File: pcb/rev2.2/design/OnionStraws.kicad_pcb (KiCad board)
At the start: 2 copper layers, 88.6 x 30 mm, 74 parts, among them J1 8P8C, J2 1x6, J3 TC2030, Q1 Si2309CDS, Q2 Si2309CDS, SW1 SW_Push, SW2 SW_Push, U1 APX803L20-29SA-7, U2 ESP32-C3-WROOM-02, U3 L7805, U4 74LVC2G07, U5 74LVC2G07_3v3, U6 AP2205-3.3

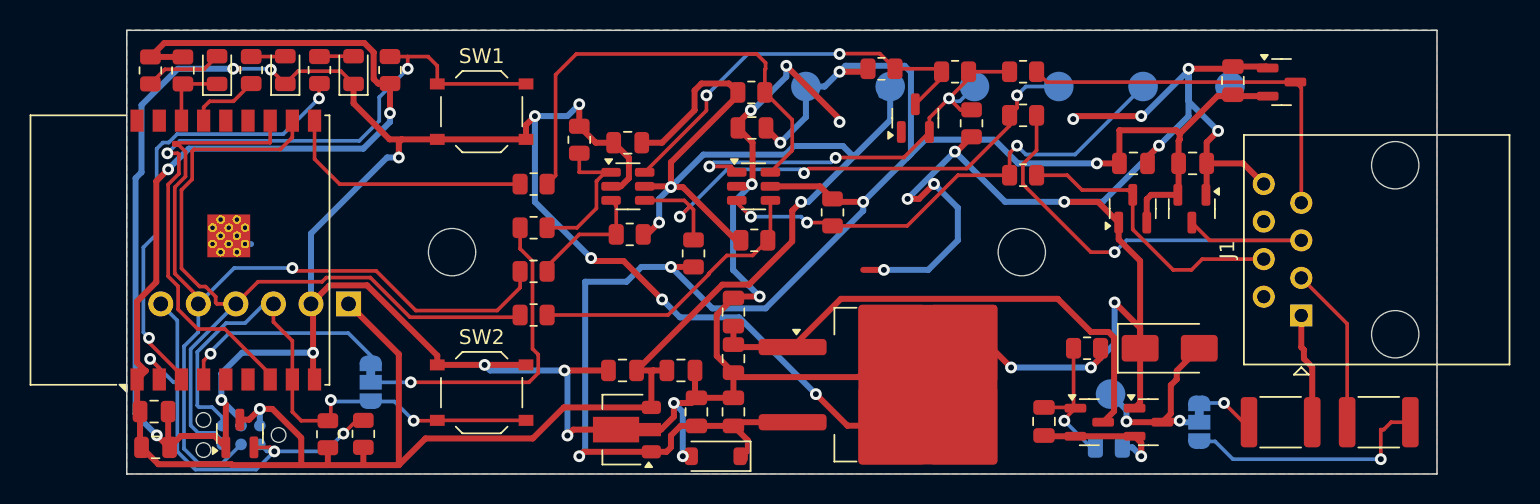
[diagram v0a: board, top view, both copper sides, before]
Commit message: fix(pcb): stage reviewed historical Rev2.2 source
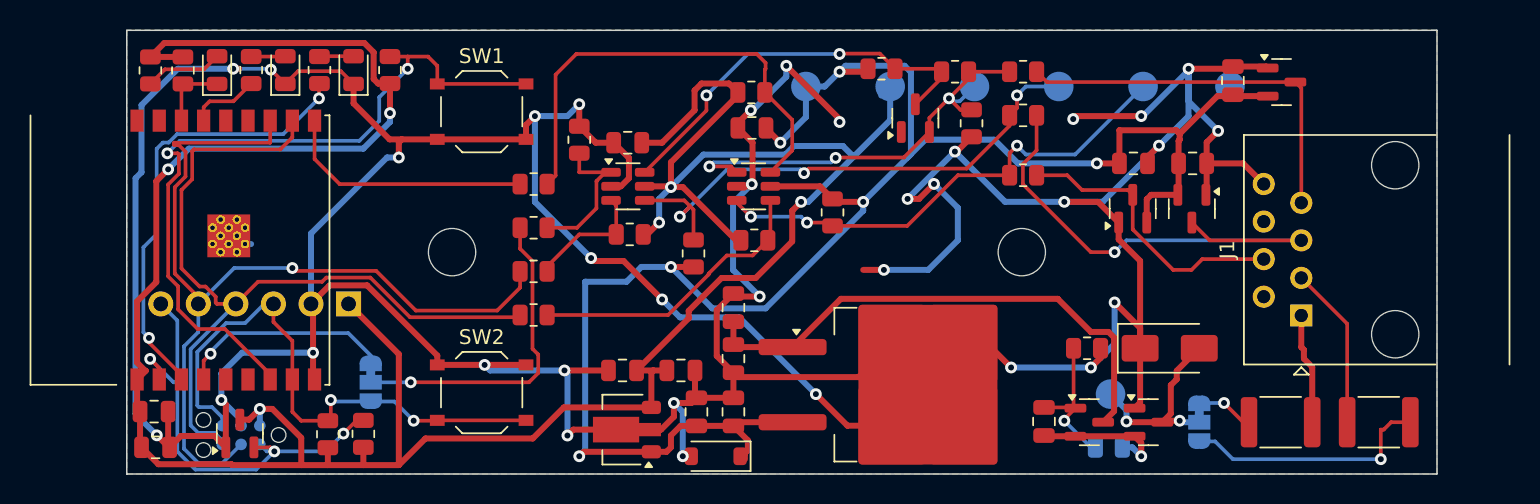
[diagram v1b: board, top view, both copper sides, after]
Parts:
- C1: footprint Capacitor_SMD:C_0805_2012Metric -> LegacyBoard:C1_C_0805_2012Metric
- C10: footprint Capacitor_SMD:C_0805_2012Metric -> LegacyBoard:C10_C_0805_2012Metric
- C11: footprint Capacitor_SMD:C_0805_2012Metric -> LegacyBoard:C11_C_0805_2012Metric
- C12: footprint Capacitor_SMD:C_0805_2012Metric -> LegacyBoard:C12_C_0805_2012Metric
- C13: footprint Capacitor_SMD:C_0805_2012Metric -> LegacyBoard:C13_C_0805_2012Metric
- C14: footprint Capacitor_SMD:C_0805_2012Metric -> LegacyBoard:C14_C_0805_2012Metric
- C2: footprint Capacitor_SMD:C_0805_2012Metric -> LegacyBoard:C2_C_0805_2012Metric
- C3: footprint Capacitor_SMD:C_0805_2012Metric -> LegacyBoard:C3_C_0805_2012Metric
- C4: footprint Capacitor_SMD:C_0805_2012Metric -> LegacyBoard:C4_C_0805_2012Metric
- C5: footprint Capacitor_SMD:C_0805_2012Metric -> LegacyBoard:C5_C_0805_2012Metric
- C6: footprint Capacitor_SMD:C_0805_2012Metric -> LegacyBoard:C6_C_0805_2012Metric
- C7: footprint Capacitor_SMD:C_0805_2012Metric -> LegacyBoard:C7_C_0805_2012Metric
- C8: footprint Capacitor_SMD:C_0805_2012Metric -> LegacyBoard:C8_C_0805_2012Metric
- C9: footprint Capacitor_SMD:C_0805_2012Metric -> LegacyBoard:C9_C_0805_2012Metric
- D1: footprint Package_TO_SOT_SMD:SOT-23 -> LegacyBoard:D1_SOT-23
- D2: footprint Package_TO_SOT_SMD:SOT-23 -> LegacyBoard:D2_SOT-23
- D3: footprint Package_TO_SOT_SMD:SOT-23 -> LegacyBoard:D3_SOT-23
- D4: footprint LED_SMD:LED_0805_2012Metric -> LegacyBoard:D4_LED_0805_2012Metric
- D5: footprint LED_SMD:LED_0805_2012Metric -> LegacyBoard:D5_LED_0805_2012Metric
- D6: footprint LED_SMD:LED_0805_2012Metric -> LegacyBoard:D6_LED_0805_2012Metric
- D7: footprint Diode_SMD:D_SMA -> LegacyBoard:D7_D_SMA
- D8: footprint Diode_SMD:D_SOD-123 -> LegacyBoard:D8_D_SOD-123
- D9: footprint Package_TO_SOT_SMD:SOT-23 -> LegacyBoard:D9_SOT-23
- F1: footprint Fuse:Fuse_1812_4532Metric -> LegacyBoard:F1_Fuse_1812_4532Metric
- F2: footprint Fuse:Fuse_1812_4532Metric -> LegacyBoard:F2_Fuse_1812_4532Metric
- H1: footprint MountingHole:MountingHole_3.2mm_M3_DIN965 -> LegacyBoard:H1_MountingHole_3.2mm_M3_DIN965
- H2: footprint MountingHole:MountingHole_3.2mm_M3_DIN965 -> LegacyBoard:H2_MountingHole_3.2mm_M3_DIN965
- J1: footprint OnionStraws:RJ45_EVERCOM_5301-8P8C_Horizontal -> LegacyBoard:J1_RJ45_EVERCOM_5301-8P8C_Horizontal
- J2: footprint Connector_PinHeader_2.54mm:PinHeader_1x06_P2.54mm_Vertical -> LegacyBoard:J2_PinHeader_1x06_P2.54mm_Vertical
- J3: footprint Connector:Tag-Connect_TC2030-IDC-NL_2x03_P1.27mm_Vertical -> LegacyBoard:J3_Tag-Connect_TC2030-IDC-NL_2x03_P1.27mm_Vertical
- JP1: footprint Jumper:SolderJumper-3_P1.3mm_Bridged12_RoundedPad1.0x1.5mm_NumberLabels -> LegacyBoard:JP1_SolderJumper-3_P1.3mm_Bridged12_RoundedPad1.0x1.5mm_NumberLabels
- JP2: footprint Jumper:SolderJumper-3_P1.3mm_Bridged12_RoundedPad1.0x1.5mm_NumberLabels -> LegacyBoard:JP2_SolderJumper-3_P1.3mm_Bridged12_RoundedPad1.0x1.5mm_NumberLabels
- Q1: footprint Package_TO_SOT_SMD:SOT-23 -> LegacyBoard:Q1_SOT-23
- Q2: footprint Package_TO_SOT_SMD:SOT-23 -> LegacyBoard:Q2_SOT-23
- R1: footprint Resistor_SMD:R_0805_2012Metric -> LegacyBoard:R1_R_0805_2012Metric
- R10: footprint Resistor_SMD:R_0805_2012Metric -> LegacyBoard:R10_R_0805_2012Metric
- R11: footprint Resistor_SMD:R_0805_2012Metric -> LegacyBoard:R11_R_0805_2012Metric
- R12: footprint Resistor_SMD:R_0805_2012Metric -> LegacyBoard:R12_R_0805_2012Metric
- R13: footprint Resistor_SMD:R_0805_2012Metric -> LegacyBoard:R13_R_0805_2012Metric
- R14: footprint Resistor_SMD:R_0805_2012Metric -> LegacyBoard:R14_R_0805_2012Metric
- R15: footprint Resistor_SMD:R_0805_2012Metric -> LegacyBoard:R15_R_0805_2012Metric
- R16: footprint Resistor_SMD:R_0805_2012Metric -> LegacyBoard:R16_R_0805_2012Metric
- R17: footprint Resistor_SMD:R_0805_2012Metric -> LegacyBoard:R17_R_0805_2012Metric
- R18: footprint Resistor_SMD:R_0805_2012Metric -> LegacyBoard:R18_R_0805_2012Metric
- R19: footprint Resistor_SMD:R_0805_2012Metric -> LegacyBoard:R19_R_0805_2012Metric
- R2: footprint Resistor_SMD:R_0805_2012Metric -> LegacyBoard:R2_R_0805_2012Metric
- R20: footprint Resistor_SMD:R_0805_2012Metric -> LegacyBoard:R20_R_0805_2012Metric
- R21: footprint Resistor_SMD:R_0805_2012Metric -> LegacyBoard:R21_R_0805_2012Metric
- R22: footprint Resistor_SMD:R_0805_2012Metric -> LegacyBoard:R22_R_0805_2012Metric
- R23: footprint Resistor_SMD:R_0805_2012Metric -> LegacyBoard:R23_R_0805_2012Metric
- R24: footprint Resistor_SMD:R_0805_2012Metric -> LegacyBoard:R24_R_0805_2012Metric
- R25: footprint Resistor_SMD:R_0805_2012Metric -> LegacyBoard:R25_R_0805_2012Metric
- R3: footprint Resistor_SMD:R_0805_2012Metric -> LegacyBoard:R3_R_0805_2012Metric
- R4: footprint Resistor_SMD:R_0805_2012Metric -> LegacyBoard:R4_R_0805_2012Metric
- R5: footprint Resistor_SMD:R_0805_2012Metric -> LegacyBoard:R5_R_0805_2012Metric
- R6: footprint Resistor_SMD:R_0805_2012Metric -> LegacyBoard:R6_R_0805_2012Metric
- R7: footprint Resistor_SMD:R_0805_2012Metric -> LegacyBoard:R7_R_0805_2012Metric
- R8: footprint Resistor_SMD:R_0805_2012Metric -> LegacyBoard:R8_R_0805_2012Metric
- R9: footprint Resistor_SMD:R_0805_2012Metric -> LegacyBoard:R9_R_0805_2012Metric
- SW1: footprint Button_Switch_SMD:SW_Push_1P1T_XKB_TS-1187A -> LegacyBoard:SW1_SW_Push_1P1T_XKB_TS-1187A
- SW2: footprint Button_Switch_SMD:SW_Push_1P1T_XKB_TS-1187A -> LegacyBoard:SW2_SW_Push_1P1T_XKB_TS-1187A
- TP1: footprint TestPoint:TestPoint_Pad_D2.0mm -> LegacyBoard:TP1_TestPoint_Pad_D2.0mm
- TP2: footprint TestPoint:TestPoint_Pad_D2.0mm -> LegacyBoard:TP2_TestPoint_Pad_D2.0mm
- TP3: footprint TestPoint:TestPoint_Pad_D2.0mm -> LegacyBoard:TP3_TestPoint_Pad_D2.0mm
- TP4: footprint TestPoint:TestPoint_Pad_D2.0mm -> LegacyBoard:TP4_TestPoint_Pad_D2.0mm
- TP5: footprint TestPoint:TestPoint_Pad_D2.0mm -> LegacyBoard:TP5_TestPoint_Pad_D2.0mm
- TP6: footprint TestPoint:TestPoint_Pad_D2.0mm -> LegacyBoard:TP6_TestPoint_Pad_D2.0mm
- TP7: footprint TestPoint:TestPoint_Pad_D2.0mm -> LegacyBoard:TP7_TestPoint_Pad_D2.0mm
- U1: footprint Package_TO_SOT_SMD:SOT-23 -> LegacyBoard:U1_SOT-23
- U2: footprint RF_Module:ESP32-C3-WROOM-02 -> LegacyBoard:U2_ESP32-C3-WROOM-02
- U3: footprint Package_TO_SOT_SMD:TO-263-2 -> LegacyBoard:U3_TO-263-2
- U4: footprint Package_TO_SOT_SMD:SOT-23-6 -> LegacyBoard:U4_SOT-23-6
- U5: footprint Package_TO_SOT_SMD:SOT-23-6 -> LegacyBoard:U5_SOT-23-6
- U6: footprint Package_TO_SOT_SMD:SOT-89-3 -> LegacyBoard:U6_SOT-89-3
- moved C10 0.30 mm to (84.0, 98.8)
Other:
- board text added: "3v3 GND BOOT EN TX RX"
- board text added: "EN TX RX BOOT GND 3v3"
- board text removed: "3v3 GND BOOT EN RX TX"
- board text removed: "EN RX TX BOOT GND 3v3"
